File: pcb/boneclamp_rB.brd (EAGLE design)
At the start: 160 x 100 mm, 68 parts, among them IC1 24C, U1 ADA4841-2YRZ, U2 LT1964ES5-5TRMPBF, U3 ADA4841-2YRZ, U4 TLV70245DBVT, U5 ADA4841-2YRZ, U6 ADA4841-2YRZ, U7 AD7682BCPZ, U8 TPS63700DRCT, U9 ADA4841-2YRZ

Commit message: Finished basic ADC module
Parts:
- removed C1, C2, C3, C4: 1 uF, rcl:C0402
- removed JP2: (no value), jumper:JP2
- removed JP3, JP4: (no value), jumper:JP1
- removed U3, U5, U6: ADA4841-2YRZ, analog-devices-01:SOIC127P600X175-8N
- added C10, C11: 10uF, rcl:C0805
- added C12, C13, C14: 0.1uF, rcl:C0805
- added R14: 1k, resistor:R0805
- added SJ6: (no value), jumper:SJ
- U1: value ADA4841-2YRZ -> AD8031ARTZ-R2; device analog-devices-01:SOIC127P600X175-8N -> analog-devices-01:SOT95P280X145-5N
- moved U1 435.1 mm to (-82.5, -306.1)
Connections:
- net SDIN_BB renamed DAC_SDI
- net SDIN_DC renamed DAC_SDID
- net SDO_DC renamed DAC_SDO
- removed net N$1: U3.8, U5.8
- removed net N$13: C4.1
- removed net N$15: U3.1, U5.1
- removed net N$2: U3.3, U5.3
- removed net N$20: JP3.1
- removed net N$24: JP4.1, U$42.1
- removed net N$26: U3.7, U5.7
- removed net N$3: U3.2, U5.2
- removed net N$4: U3.5, U5.5
- removed net N$5: U3.6, U5.6
- removed net N$6: U3.4, U5.4
- removed net VDD_2: U7.1
- removed net VIO: U7.15
- removed net VREF_2.5V: JP3.2, JP4.2
- new net ADC_SDO: SJ6.2
- new net N$28: C11.1, R14.2, U7.2
- new net N$29: C10.1, R14.1, U1.3
- new net N$34: C14.1, U7.3
- new net VCOM: U7.10
- new net VREF: U1.1, U1.4
- new net _ADC_A: U7.16
- new net _ADC_B: U7.18
- new net _ADC_C: U7.7
- new net _ADC_D: U7.9
- net +VS: no longer U1.8, U6.8
- net -VS: no longer U1.4, U6.4
- net AGND: now also C10.2, C11.2, C12.2, C13.2, C14.2, U1.2, U7.21, U7.4, U7.5; no longer C1.2, C2.2, C3.2, C4.2
- net DGND: no longer JP2.3
- net N$10: now also U7.13; no longer C2.1
- net N$11: now also U7.12; no longer C1.1
- net N$12: now also U7.11; no longer JP2.2
- net N$9: now also SJ6.1; no longer C3.1
- net VDD: now also C13.1, U1.5, U7.1
- net VDRIVE: now also C12.1, U7.15; no longer JP2.1

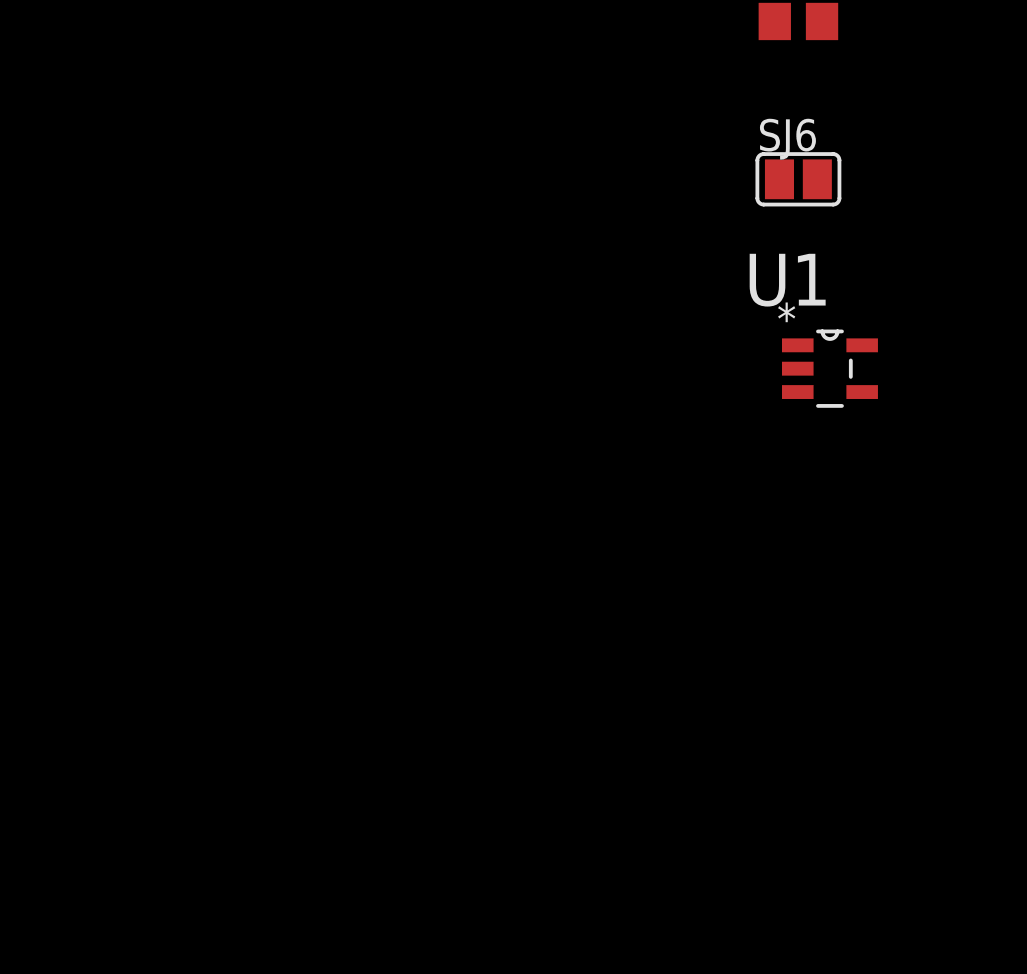
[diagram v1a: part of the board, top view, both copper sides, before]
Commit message: Added buffered VREF divider, which feeds back into ADC to get bipolar input swing.
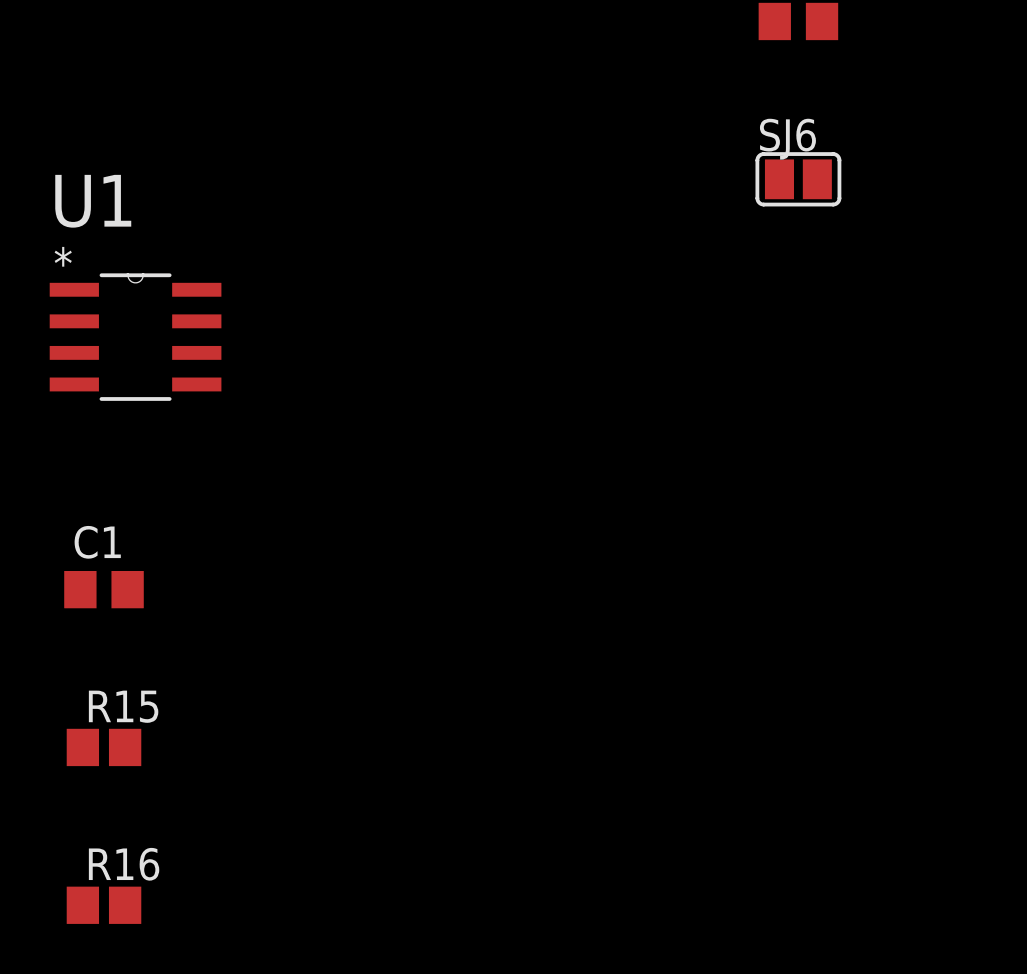
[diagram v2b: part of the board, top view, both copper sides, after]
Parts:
- added C1: 10uF, rcl:C0805
- added R15, R16: 10k,1%, resistor:R0805
- U1: value AD8031ARTZ-R2 -> AD8032ARZ-REEL7; device analog-devices-01:SOT95P280X145-5N -> analog-devices-02:SOIC127P600X175-8N
- moved U1 28.0 mm to (-110.5, -304.8)
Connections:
- new net N$4: C1.1, R15.2, R16.1, U1.5
- net AGND: now also C1.2, R16.2, U1.4; no longer U1.2
- net I2C2_SCL: now also TP5.TP
- net VCOM: now also U1.6, U1.7
- net VDD: now also U1.8; no longer U1.5
- net VREF: now also R15.1, U1.2; no longer U1.4
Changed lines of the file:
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@@
 <element name="C14" library="rcl" package="C0805" value="0.1uF" x="-83.82" y="-292.1"/>
 <element name="SJ6" library="jumper" package="SJ" value="" x="-83.82" y="-298.45"/>
-<element name="U1" library="analog-devices-01" package="SOT95P280X145-5N" value="AD8031ARTZ-R2" x="-82.55" y="-306.07">
-<attribute name="PACKAGE" value="SOT23-5" x="-82.55" y="-306.07" size="1.778" layer="27" display="off"/>
-<attribute name="OC_NEWARK" value="19M8875" x="-82.55" y="-306.07" size="1.778" layer="27" display="off"/>
-<attribute name="MPN" value="AD8031ARTZ-R2" x="-82.55" y="-306.07" size="1.778" layer="27" display="off"/>
-<attribute name="SUPPLIER" value="Analog Devices" x="-82.55" y="-306.07" size="1.778" layer="27" display="off"/>
-<attribute name="OC_FARNELL" value="1319421" x="-82.55" y="-306.07" size="1.778" layer="27" display="off"/>
+<element name="U1" library="analog-devices-02" package="SOIC127P600X175-8N" value="AD8032ARZ-REEL7" x="-110.49" y="-304.8">
+<attribute name="PACKAGE" value="SOIC-8" x="-110.49" y="-304.8" size="1.778" layer="27" display="off"/>
+<attribute name="OC_NEWARK" value="82H2954" x="-110.49" y="-304.8" size="1.778" layer="27" display="off"/>
+<attribute name="MPN" value="AD8032ARZ-REEL7" x="-110.49" y="-304.8" size="1.778" layer="27" display="off"/>
+<attribute name="SUPPLIER" value="Analog Devices" x="-110.49" y="-304.8" size="1.778" layer="27" display="off"/>
+<attribute name="OC_FARNELL" value="unknown" x="-110.49" y="-304.8" size="1.778" layer="27" display="off"/>
 </element>
+<element name="C1" library="rcl" package="C0805" value="10uF" x="-111.76" y="-314.96"/>
+<element name="R15" library="resistor" package="R0805" value="10k,1%" x="-111.76" y="-321.31"/>
+<element name="R16" library="resistor" package="R0805" value="10k,1%" x="-111.76" y="-327.66"/>
 </elements>
 <signals>
@@
 <contactref element="C13" pad="1"/>
 <contactref element="U7" pad="20"/>
-<contactref element="U1" pad="5"/>
-<wire x1="-84.77" y1="-285.75" x2="-81.2546" y2="-305.1302" width="0" layer="19" extent="1-1"/>
+<contactref element="U1" pad="8"/>
+<wire x1="-84.77" y1="-285.75" x2="-108.0262" y2="-302.895" width="0" layer="19" extent="1-1"/>
 <wire x1="-84.77" y1="-236.22" x2="-84.77" y2="-285.75" width="0" layer="19" extent="1-1"/>
 <wire x1="-81.2546" y1="-220.0402" x2="-84.77" y2="-236.22" width="0" layer="19" extent="1-1"/>
@@
 <contactref element="U7" pad="21"/>
 <contactref element="C14" pad="2"/>
-<contactref element="U1" pad="2"/>
+<contactref element="U1" pad="4"/>
+<contactref element="R16" pad="2"/>
+<contactref element="C1" pad="2"/>
 <wire x1="-82.87" y1="-177.8" x2="-83.7692" y2="-167.9702" width="0" layer="19" extent="1-1"/>
 <wire x1="-82.87" y1="-184.15" x2="-82.87" y2="-177.8" width="0" layer="19" extent="1-1"/>
@@
 <wire x1="-82.87" y1="-285.75" x2="-82.87" y2="-279.4" width="0" layer="19" extent="1-1"/>
 <wire x1="-82.87" y1="-292.1" x2="-82.87" y2="-285.75" width="0" layer="19" extent="1-1"/>
-<wire x1="-83.8454" y1="-306.07" x2="-82.87" y2="-292.1" width="0" layer="19" extent="1-1"/>
+<wire x1="-112.9538" y1="-306.705" x2="-82.87" y2="-292.1" width="0" layer="19" extent="1-1"/>
+<wire x1="-110.81" y1="-314.96" x2="-112.9538" y2="-306.705" width="0" layer="19" extent="1-1"/>
+<wire x1="-110.91" y1="-327.66" x2="-110.81" y2="-314.96" width="0" layer="19" extent="1-1"/>
 <wire x1="1.905" y1="19.05" x2="-81.0768" y2="-61.468" width="0" layer="19" extent="1-1"/>
 <wire x1="4.445" y1="19.05" x2="1.905" y2="19.05" width="0" layer="19" extent="1-1"/>
@@
 <contactref element="R10" pad="1"/>
 <contactref element="IC1" pad="6"/>
-<wire x1="26.035" y1="30.54" x2="11.85" y2="0" width="0" layer="19" extent="1-1"/>
-<wire x1="52.705" y1="41.91" x2="26.035" y2="30.54" width="0" layer="19" extent="1-1"/>
+<contactref element="TP5" pad="TP"/>
+<wire x1="26.035" y1="30.54" x2="52.705" y2="41.91" width="0" layer="19" extent="1-1"/>
+<wire x1="11.85" y1="0" x2="26.035" y2="30.54" width="0" layer="19" extent="1-1"/>
+<wire x1="-85.09" y1="-208.28" x2="11.85" y2="0" width="0" layer="19" extent="1-1"/>
 </signal>
 <signal name="I2C2_SDA">
@@
 <contactref element="C10" pad="1"/>
 <contactref element="U1" pad="3"/>
-<wire x1="-84.67" y1="-266.7" x2="-83.8454" y2="-307.0098" width="0" layer="19" extent="1-1"/>
+<wire x1="-84.67" y1="-266.7" x2="-112.9538" y2="-305.435" width="0" layer="19" extent="1-1"/>
 <wire x1="-84.77" y1="-254" x2="-84.67" y2="-266.7" width="0" layer="19" extent="1-1"/>
 </signal>
@@
 <signal name="VCOM">
 <contactref element="U7" pad="10"/>
+<contactref element="U1" pad="6"/>
+<contactref element="U1" pad="7"/>
+<wire x1="-108.0262" y1="-304.165" x2="-108.0262" y2="-305.435" width="0" layer="19" extent="1-1"/>
+<wire x1="37.8206" y1="59.182" x2="-108.0262" y2="-304.165" width="0" layer="19" extent="1-1"/>
 </signal>
 <signal name="N$9">
@@
 </signal>
 <signal name="VREF">
-<contactref element="U1" pad="4"/>
 <contactref element="U1" pad="1"/>
-<wire x1="-81.2546" y1="-307.0098" x2="-83.8454" y2="-305.1302" width="0" layer="19" extent="1-1"/>
+<contactref element="U1" pad="2"/>
+<contactref element="R15" pad="1"/>
+<wire x1="-112.9538" y1="-304.165" x2="-112.61" y2="-321.31" width="0" layer="19" extent="1-1"/>
+<wire x1="-112.9538" y1="-302.895" x2="-112.9538" y2="-304.165" width="0" layer="19" extent="1-1"/>
+</signal>
+<signal name="N$4">
+<contactref element="R16" pad="1"/>
+<contactref element="R15" pad="2"/>
+<contactref element="C1" pad="1"/>
+<contactref element="U1" pad="5"/>
+<wire x1="-110.91" y1="-321.31" x2="-112.61" y2="-327.66" width="0" layer="19" extent="1-1"/>
+<wire x1="-112.71" y1="-314.96" x2="-110.91" y2="-321.31" width="0" layer="19" extent="1-1"/>
+<wire x1="-108.0262" y1="-306.705" x2="-112.71" y2="-314.96" width="0" layer="19" extent="1-1"/>
 </signal>
 </signals>

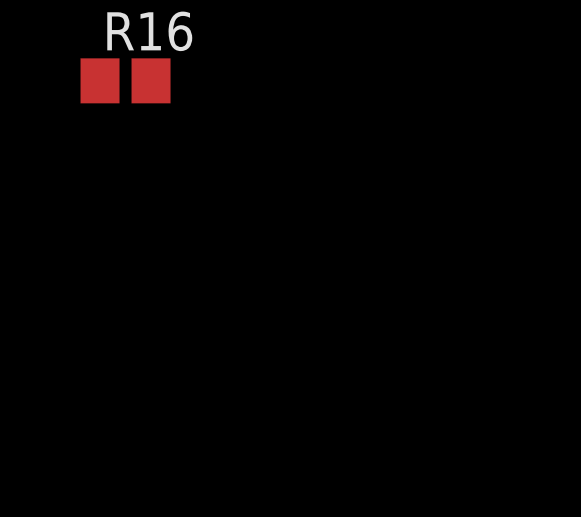
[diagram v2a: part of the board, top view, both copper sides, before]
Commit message: Finished digital input to DAC
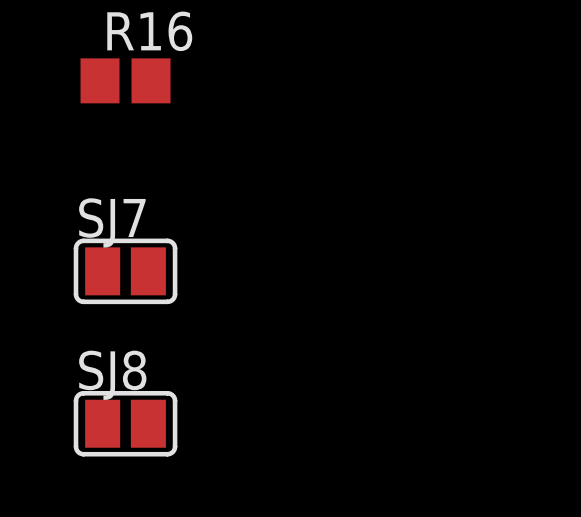
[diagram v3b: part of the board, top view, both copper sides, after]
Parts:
- added SJ7, SJ8: (no value), jumper:SJ
- U$42: value AD5686RARUZ -> AD5686
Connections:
- net N$10 renamed ADC_SCLK
- new net ADC_SDI: SJ7.1
- new net ADC_SDID: SJ8.1
- new net DAC_CS: U$42.13
- new net DAC_RST: U$42.15
- new net DAC_SCLK: U$42.12
- net AGND: now also U$42.10, U$42.16, U$42.4, U$42.9
- net N$11: now also SJ7.2, SJ8.2
- net VREF: now also U$42.1
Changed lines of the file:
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@@
 <element name="R11" library="rcl" package="R0603" value="10k" x="12.7" y="-5.08"/>
 <element name="SJ5" library="jumper" package="SJ" value="" x="12.7" y="-11.43"/>
-<element name="U$42" library="analog-devices-02" package="MO-153-AB" value="AD5686RARUZ" x="17.78" y="60.96"/>
+<element name="U$42" library="analog-devices-02" package="MO-153-AB" value="AD5686" x="17.78" y="60.96"/>
 <element name="U7" library="analog-devices-02" package="QFN50P400X400X100-21N" value="AD7682BCPZ" x="36.83" y="60.96">
 <attribute name="PACKAGE" value="20-LFCSP" x="36.83" y="60.96" size="1.778" layer="27" display="off"/>
@@
 <element name="R15" library="resistor" package="R0805" value="10k,1%" x="-111.76" y="-321.31"/>
 <element name="R16" library="resistor" package="R0805" value="10k,1%" x="-111.76" y="-327.66"/>
+<element name="SJ7" library="jumper" package="SJ" value="" x="-111.76" y="-334.01"/>
+<element name="SJ8" library="jumper" package="SJ" value="" x="-111.76" y="-339.09"/>
 </elements>
 <signals>
@@
 <contactref element="R16" pad="2"/>
 <contactref element="C1" pad="2"/>
+<contactref element="U$42" pad="4"/>
+<contactref element="U$42" pad="10"/>
+<contactref element="U$42" pad="9"/>
+<contactref element="U$42" pad="16"/>
 <wire x1="-82.87" y1="-177.8" x2="-83.7692" y2="-167.9702" width="0" layer="19" extent="1-1"/>
 <wire x1="-82.87" y1="-184.15" x2="-82.87" y2="-177.8" width="0" layer="19" extent="1-1"/>
@@
 <wire x1="7.94" y1="63.5" x2="9.84" y2="59.69" width="0" layer="19" extent="1-1"/>
 <wire x1="9.84" y1="67.31" x2="7.94" y2="63.5" width="0" layer="19" extent="1-1"/>
-<wire x1="25.4" y1="57.658" x2="9.84" y2="59.69" width="0" layer="19" extent="1-1"/>
+<wire x1="14.9606" y1="61.2902" x2="9.84" y2="59.69" width="0" layer="19" extent="1-1"/>
+<wire x1="20.5994" y1="63.246" x2="14.9606" y2="61.2902" width="0" layer="19" extent="1-1"/>
+<wire x1="20.5994" y1="59.3344" x2="20.5994" y2="63.246" width="0" layer="19" extent="1-1"/>
+<wire x1="20.5994" y1="58.674" x2="20.5994" y2="59.3344" width="0" layer="19" extent="1-1"/>
+<wire x1="25.4" y1="57.658" x2="20.5994" y2="58.674" width="0" layer="19" extent="1-1"/>
 <wire x1="35.052" y1="59.9694" x2="25.4" y2="57.658" width="0" layer="19" extent="1-1"/>
 <wire x1="35.052" y1="60.452" x2="35.052" y2="59.9694" width="0" layer="19" extent="1-1"/>
@@
 <contactref element="SJ6" pad="2"/>
 </signal>
-<signal name="N$10">
+<signal name="ADC_SCLK">
 <contactref element="U7" pad="13"/>
 </signal>
 <signal name="N$11">
 <contactref element="U7" pad="12"/>
+<contactref element="SJ8" pad="2"/>
+<contactref element="SJ7" pad="2"/>
+<wire x1="-110.998" y1="-334.01" x2="-110.998" y2="-339.09" width="0" layer="19" extent="1-1"/>
+<wire x1="38.608" y1="60.452" x2="-110.998" y2="-334.01" width="0" layer="19" extent="1-1"/>
 </signal>
 <signal name="N$12">
@@
 <contactref element="U1" pad="2"/>
 <contactref element="R15" pad="1"/>
+<contactref element="U$42" pad="1"/>
 <wire x1="-112.9538" y1="-304.165" x2="-112.61" y2="-321.31" width="0" layer="19" extent="1-1"/>
 <wire x1="-112.9538" y1="-302.895" x2="-112.9538" y2="-304.165" width="0" layer="19" extent="1-1"/>
+<wire x1="14.9606" y1="63.246" x2="-112.9538" y2="-302.895" width="0" layer="19" extent="1-1"/>
 </signal>
 <signal name="N$4">
@@
 <wire x1="-108.0262" y1="-306.705" x2="-112.71" y2="-314.96" width="0" layer="19" extent="1-1"/>
 </signal>
+<signal name="ADC_SDID">
+<contactref element="SJ8" pad="1"/>
+</signal>
+<signal name="ADC_SDI">
+<contactref element="SJ7" pad="1"/>
+</signal>
+<signal name="DAC_SCLK">
+<contactref element="U$42" pad="12"/>
+</signal>
+<signal name="DAC_RST">
+<contactref element="U$42" pad="15"/>
+</signal>
+<signal name="DAC_CS">
+<contactref element="U$42" pad="13"/>
+</signal>
 </signals>

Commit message: Minor schematic edit
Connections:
- new net _DAC_A: C15.1, R1.2, TP4.TP, U$42.3
- new net _DAC_B: C16.1, R2.2, TP3.TP, U$42.2
- new net _DAC_C: C17.1, R3.2, TP2.TP, U$42.6
- new net _DAC_D: C18.1, R4.2, TP1.TP, U$42.7
- net DAC_A: no longer C15.1, R1.2, TP4.TP, U$42.3
- net DAC_B: no longer C16.1, R2.2, TP3.TP, U$42.2
- net DAC_C: no longer C17.1, R3.2, TP2.TP, U$42.6
- net DAC_D: no longer C18.1, R4.2, TP1.TP, U$42.7
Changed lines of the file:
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@@
 </signal>
 <signal name="DAC_A">
-<contactref element="R1" pad="2"/>
-<contactref element="C15" pad="1"/>
-<contactref element="TP4" pad="TP"/>
-<contactref element="U$42" pad="3"/>
 <contactref element="JP5" pad="3"/>
-<wire x1="8.89" y1="29.21" x2="14.9606" y2="61.9252" width="0" layer="19" extent="1-1"/>
-<wire x1="9.84" y1="71.12" x2="8.89" y2="29.21" width="0" layer="19" extent="1-1"/>
-<wire x1="7.94" y1="74.93" x2="9.84" y2="71.12" width="0" layer="19" extent="1-1"/>
-<wire x1="16.51" y1="77.47" x2="14.9606" y2="61.9252" width="0" layer="19" extent="1-1"/>
 </signal>
 <signal name="DAC_B">
-<contactref element="R2" pad="2"/>
-<contactref element="C16" pad="1"/>
-<contactref element="TP3" pad="TP"/>
-<contactref element="U$42" pad="2"/>
 <contactref element="JP5" pad="5"/>
-<wire x1="8.89" y1="34.29" x2="14.9606" y2="62.5856" width="0" layer="19" extent="1-1"/>
-<wire x1="9.84" y1="63.5" x2="8.89" y2="34.29" width="0" layer="19" extent="1-1"/>
-<wire x1="7.94" y1="67.31" x2="9.84" y2="63.5" width="0" layer="19" extent="1-1"/>
-<wire x1="19.05" y1="77.47" x2="14.9606" y2="62.5856" width="0" layer="19" extent="1-1"/>
 </signal>
 <signal name="DAC_C">
-<contactref element="TP2" pad="TP"/>
-<contactref element="R3" pad="2"/>
-<contactref element="C17" pad="1"/>
-<contactref element="U$42" pad="6"/>
 <contactref element="JP5" pad="7"/>
-<wire x1="8.89" y1="39.37" x2="14.9606" y2="59.9948" width="0" layer="19" extent="1-1"/>
-<wire x1="9.84" y1="55.88" x2="8.89" y2="39.37" width="0" layer="19" extent="1-1"/>
-<wire x1="7.94" y1="59.69" x2="9.84" y2="55.88" width="0" layer="19" extent="1-1"/>
-<wire x1="21.59" y1="77.47" x2="14.9606" y2="59.9948" width="0" layer="19" extent="1-1"/>
 </signal>
 <signal name="DAC_D">
-<contactref element="R4" pad="2"/>
-<contactref element="C18" pad="1"/>
-<contactref element="TP1" pad="TP"/>
-<contactref element="U$42" pad="7"/>
 <contactref element="JP5" pad="9"/>
-<wire x1="8.89" y1="44.45" x2="14.9606" y2="59.3344" width="0" layer="19" extent="1-1"/>
-<wire x1="9.84" y1="48.26" x2="8.89" y2="44.45" width="0" layer="19" extent="1-1"/>
-<wire x1="7.94" y1="52.07" x2="9.84" y2="48.26" width="0" layer="19" extent="1-1"/>
-<wire x1="24.13" y1="77.47" x2="14.9606" y2="59.3344" width="0" layer="19" extent="1-1"/>
 </signal>
 <signal name="AGND">
@@
 <contactref element="U$42" pad="13"/>
 </signal>
+<signal name="_DAC_D">
+<contactref element="R4" pad="2"/>
+<contactref element="C18" pad="1"/>
+<contactref element="TP1" pad="TP"/>
+<contactref element="U$42" pad="7"/>
+<wire x1="7.94" y1="52.07" x2="14.9606" y2="59.3344" width="0" layer="19" extent="1-1"/>
+<wire x1="9.84" y1="48.26" x2="7.94" y2="52.07" width="0" layer="19" extent="1-1"/>
+<wire x1="8.89" y1="44.45" x2="9.84" y2="48.26" width="0" layer="19" extent="1-1"/>
+</signal>
+<signal name="_DAC_C">
+<contactref element="TP2" pad="TP"/>
+<contactref element="R3" pad="2"/>
+<contactref element="C17" pad="1"/>
+<contactref element="U$42" pad="6"/>
+<wire x1="9.84" y1="55.88" x2="14.9606" y2="59.9948" width="0" layer="19" extent="1-1"/>
+<wire x1="7.94" y1="59.69" x2="9.84" y2="55.88" width="0" layer="19" extent="1-1"/>
+<wire x1="8.89" y1="39.37" x2="9.84" y2="55.88" width="0" layer="19" extent="1-1"/>
+</signal>
+<signal name="_DAC_B">
+<contactref element="R2" pad="2"/>
+<contactref element="C16" pad="1"/>
+<contactref element="TP3" pad="TP"/>
+<contactref element="U$42" pad="2"/>
+<wire x1="9.84" y1="63.5" x2="7.94" y2="67.31" width="0" layer="19" extent="1-1"/>
+<wire x1="14.9606" y1="62.5856" x2="9.84" y2="63.5" width="0" layer="19" extent="1-1"/>
+<wire x1="8.89" y1="34.29" x2="14.9606" y2="62.5856" width="0" layer="19" extent="1-1"/>
+</signal>
+<signal name="_DAC_A">
+<contactref element="R1" pad="2"/>
+<contactref element="C15" pad="1"/>
+<contactref element="TP4" pad="TP"/>
+<contactref element="U$42" pad="3"/>
+<wire x1="9.84" y1="71.12" x2="7.94" y2="74.93" width="0" layer="19" extent="1-1"/>
+<wire x1="14.9606" y1="61.9252" x2="9.84" y2="71.12" width="0" layer="19" extent="1-1"/>
+<wire x1="8.89" y1="29.21" x2="14.9606" y2="61.9252" width="0" layer="19" extent="1-1"/>
+</signal>
 </signals>
